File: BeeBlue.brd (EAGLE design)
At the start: 31.7 x 24.4 mm, 3 parts, among them U1 HC_05

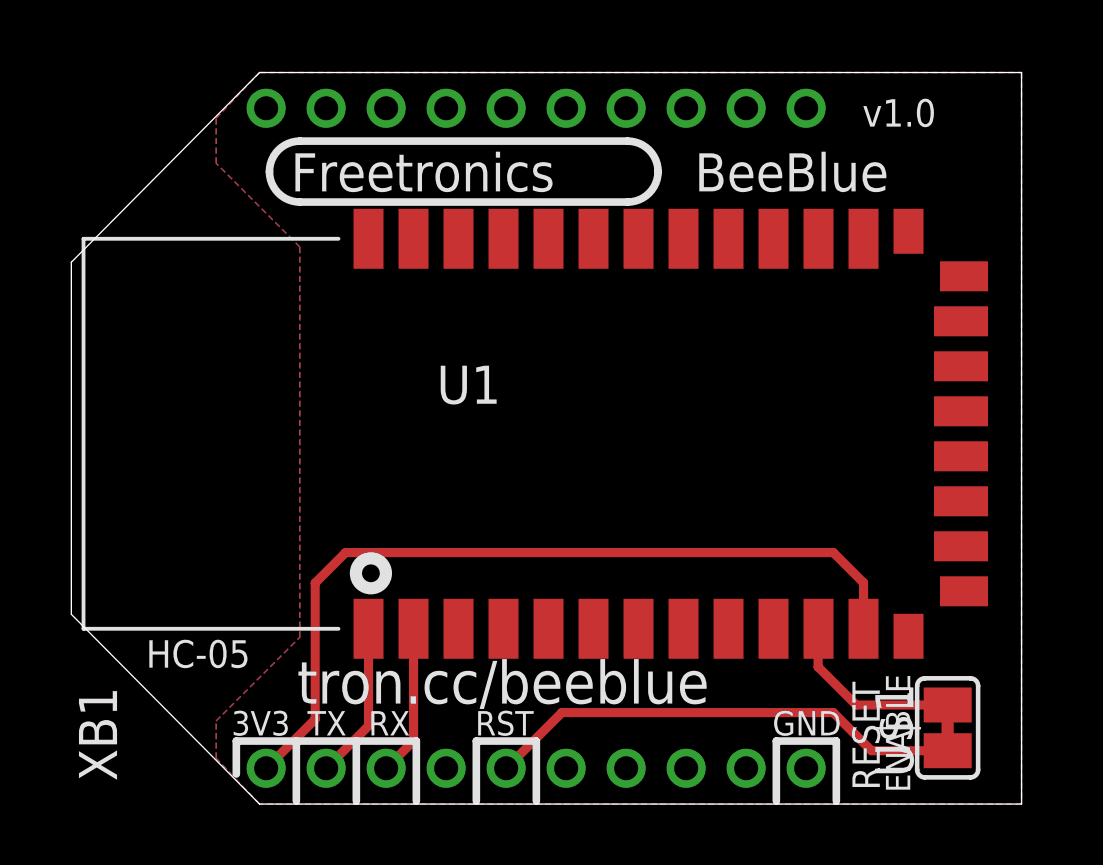
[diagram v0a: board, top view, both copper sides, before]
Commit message: Added jumper for setting command mode
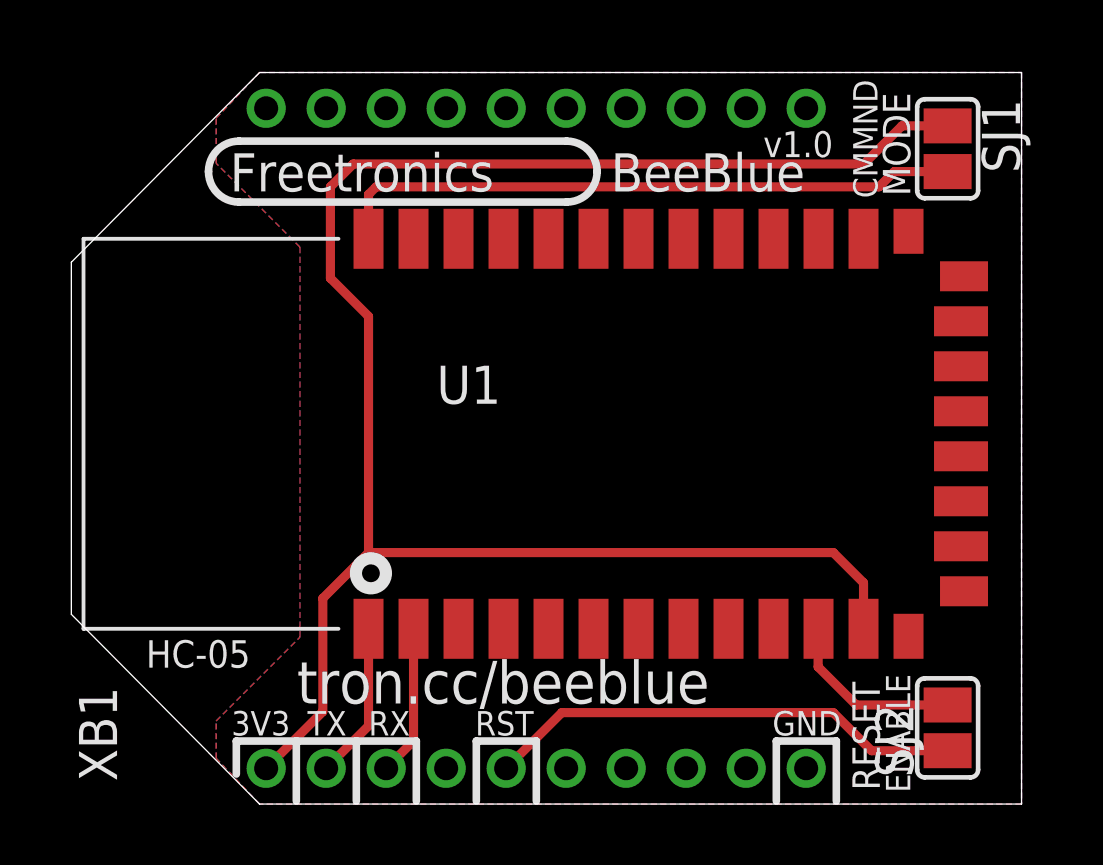
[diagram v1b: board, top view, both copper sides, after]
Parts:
- removed U$1: SJCN, freetronics-jon:SJC
- added SJ1: COMMAND MODE, freetronics-jon:SJ
- added SJ2: RESET ENABLE, freetronics-jon:SJ
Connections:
- new net N$1: SJ1.2, U1.34
- net N$4: now also SJ1.1
- net N$5: now also SJ2.2; no longer U$1.2
- net N$6: now also SJ2.1; no longer U$1.1
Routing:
- net N$4: track 27.5 -> 61.2 mm
- net N$1: track 0.00 -> 21.1 mm
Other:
- board text added: "CMMND"
- board text added: "MODE"
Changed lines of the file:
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@@
 <wire x1="6.2738" y1="24.384" x2="0" y2="18.0594" width="0" layer="20"/>
 <wire x1="0" y1="18.0594" x2="0" y2="6.3246" width="0" layer="20"/>
-<text x="7.3152" y="20.4216" size="1.27" layer="21" font="vector" ratio="15">Freetronics</text>
-<text x="26.3652" y="22.5806" size="0.9144" layer="21" font="vector" ratio="15">v1.0</text>
+<text x="5.2832" y="20.4216" size="1.27" layer="21" font="vector" ratio="15">Freetronics</text>
+<text x="23.0632" y="21.5646" size="0.8636" layer="21" font="vector" ratio="15">v1.0</text>
 <text x="9.906" y="2.286" size="0.8128" layer="21" ratio="15">RX</text>
 <text x="7.874" y="2.286" size="0.8128" layer="21" ratio="15">TX</text>
@@
 <text x="5.334" y="2.286" size="0.8128" layer="21" ratio="15">3V3</text>
 <text x="13.462" y="2.286" size="0.8128" layer="21" ratio="15">RST</text>
-<text x="20.7772" y="20.4216" size="1.27" layer="21" font="vector" ratio="15">BeeBlue</text>
+<text x="17.9832" y="20.4216" size="1.27" layer="21" font="vector" ratio="15">BeeBlue</text>
 <text x="7.5212" y="3.35" size="1.4224" layer="21" font="vector" ratio="15">tron.cc/beeblue</text>
-<wire x1="7.62" y1="22.098" x2="18.542" y2="22.098" width="0.254" layer="21"/>
-<wire x1="18.542" y1="22.098" x2="19.558" y2="21.082" width="0.254" layer="21" curve="-90"/>
-<wire x1="19.558" y1="21.082" x2="18.542" y2="20.066" width="0.254" layer="21" curve="-90"/>
-<wire x1="18.542" y1="20.066" x2="7.62" y2="20.066" width="0.254" layer="21"/>
-<wire x1="7.62" y1="20.066" x2="6.604" y2="21.082" width="0.254" layer="21" curve="-90"/>
-<wire x1="6.604" y1="21.082" x2="7.62" y2="22.098" width="0.254" layer="21" curve="-90"/>
+<wire x1="5.588" y1="22.098" x2="16.51" y2="22.098" width="0.254" layer="21"/>
+<wire x1="16.51" y1="22.098" x2="17.526" y2="21.082" width="0.254" layer="21" curve="-90"/>
+<wire x1="17.526" y1="21.082" x2="16.51" y2="20.066" width="0.254" layer="21" curve="-90"/>
+<wire x1="16.51" y1="20.066" x2="5.588" y2="20.066" width="0.254" layer="21"/>
+<wire x1="5.588" y1="20.066" x2="4.572" y2="21.082" width="0.254" layer="21" curve="-90"/>
+<wire x1="4.572" y1="21.082" x2="5.588" y2="22.098" width="0.254" layer="21" curve="-90"/>
 <text x="2.4892" y="4.5466" size="0.9144" layer="21" font="vector" ratio="15">HC-05</text>
 <text x="26.9494" y="0.4572" size="0.9144" layer="21" font="vector" ratio="15" rot="R90">RESET</text>
@@
 <text x="30.1752" y="14.1986" size="1.4224" layer="22" font="vector" ratio="15" rot="MR0">tron.cc/beeblue</text>
 <text x="25.3492" y="5.0546" size="1.4224" layer="22" font="vector" ratio="15" rot="MR0">SKU: BEEBLUE</text>
+<text x="26.8732" y="20.193" size="0.8128" layer="21" font="vector" ratio="15" rot="R90">CMMND</text>
+<text x="27.9654" y="20.2692" size="0.9144" layer="21" font="vector" ratio="15" rot="R90">MODE</text>
 </plain>
 <attributes>
@@
 </element>
 <element name="U1" library="freetronics-jon" package="BLUETOOTH_SMD" value="HC_05" x="14.986" y="12.192"/>
-<element name="U$1" library="freetronics-jon" package="SJC" value="SJCN" x="29.21" y="2.54" rot="R90"/>
+<element name="SJ2" library="freetronics-jon" package="SJ" value="RESET ENABLE" x="29.21" y="2.54" rot="R90"/>
+<element name="SJ1" library="freetronics-jon" package="SJ" value="COMMAND MODE" x="29.21" y="21.844" rot="R270"/>
 </elements>
 <signals>
@@
 <contactref element="U1" pad="12"/>
 <contactref element="XB1" pad="1"/>
-<wire x1="6.494" y1="1.192" x2="8.128" y2="2.826" width="0.3048" layer="1"/>
-<wire x1="8.128" y1="2.826" x2="8.128" y2="7.366" width="0.3048" layer="1"/>
-<wire x1="8.128" y1="7.366" x2="9.144" y2="8.382" width="0.3048" layer="1"/>
-<wire x1="9.144" y1="8.382" x2="25.4" y2="8.382" width="0.3048" layer="1"/>
+<wire x1="6.494" y1="1.192" x2="8.382" y2="3.08" width="0.3048" layer="1"/>
+<wire x1="8.382" y1="3.08" x2="8.382" y2="6.858" width="0.3048" layer="1"/>
+<wire x1="8.382" y1="6.858" x2="9.906" y2="8.382" width="0.3048" layer="1"/>
+<wire x1="9.906" y1="8.382" x2="25.4" y2="8.382" width="0.3048" layer="1"/>
 <wire x1="25.4" y1="8.382" x2="26.406" y2="7.376" width="0.3048" layer="1"/>
 <wire x1="26.406" y1="7.376" x2="26.406" y2="5.842" width="0.3048" layer="1"/>
+<contactref element="SJ1" pad="1"/>
+<wire x1="29.21" y1="22.606" x2="27.686" y2="22.606" width="0.3048" layer="1"/>
+<wire x1="27.686" y1="22.606" x2="26.416" y2="21.336" width="0.3048" layer="1"/>
+<wire x1="26.416" y1="21.336" x2="9.398" y2="21.336" width="0.3048" layer="1"/>
+<wire x1="9.398" y1="21.336" x2="8.636" y2="20.574" width="0.3048" layer="1"/>
+<wire x1="8.636" y1="20.574" x2="8.636" y2="17.526" width="0.3048" layer="1"/>
+<wire x1="8.636" y1="17.526" x2="9.906" y2="16.256" width="0.3048" layer="1"/>
+<wire x1="9.906" y1="16.256" x2="9.906" y2="8.382" width="0.3048" layer="1"/>
 </signal>
 <signal name="N$5">
-<contactref element="U$1" pad="2"/>
+<contactref element="SJ2" pad="2"/>
 <contactref element="U1" pad="11"/>
 <wire x1="29.21" y1="3.302" x2="26.162" y2="3.302" width="0.3048" layer="1"/>
@@
 </signal>
 <signal name="N$6">
-<contactref element="U$1" pad="1"/>
+<contactref element="SJ2" pad="1"/>
 <contactref element="XB1" pad="5"/>
 <wire x1="29.21" y1="1.778" x2="26.67" y2="1.778" width="0.3048" layer="1"/>
@@
 <wire x1="16.35" y1="3.048" x2="14.494" y2="1.192" width="0.3048" layer="1"/>
 </signal>
+<signal name="N$1">
+<contactref element="SJ1" pad="2"/>
+<contactref element="U1" pad="34"/>
+<wire x1="29.21" y1="21.082" x2="27.432" y2="21.082" width="0.3048" layer="1"/>
+<wire x1="27.432" y1="21.082" x2="26.924" y2="20.574" width="0.3048" layer="1"/>
+<wire x1="26.924" y1="20.574" x2="10.16" y2="20.574" width="0.3048" layer="1"/>
+<wire x1="10.16" y1="20.574" x2="9.906" y2="20.32" width="0.3048" layer="1"/>
+<wire x1="9.906" y1="20.32" x2="9.906" y2="18.842" width="0.3048" layer="1"/>
+</signal>
 </signals>
